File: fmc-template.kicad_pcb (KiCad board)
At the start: 6 copper layers, 84 x 69 mm, 31 parts, among them J19 WP Jumper, P1 ASP-134488-01, Q1 FDN335N, Q2 FDN335N, U9 AT24C64D

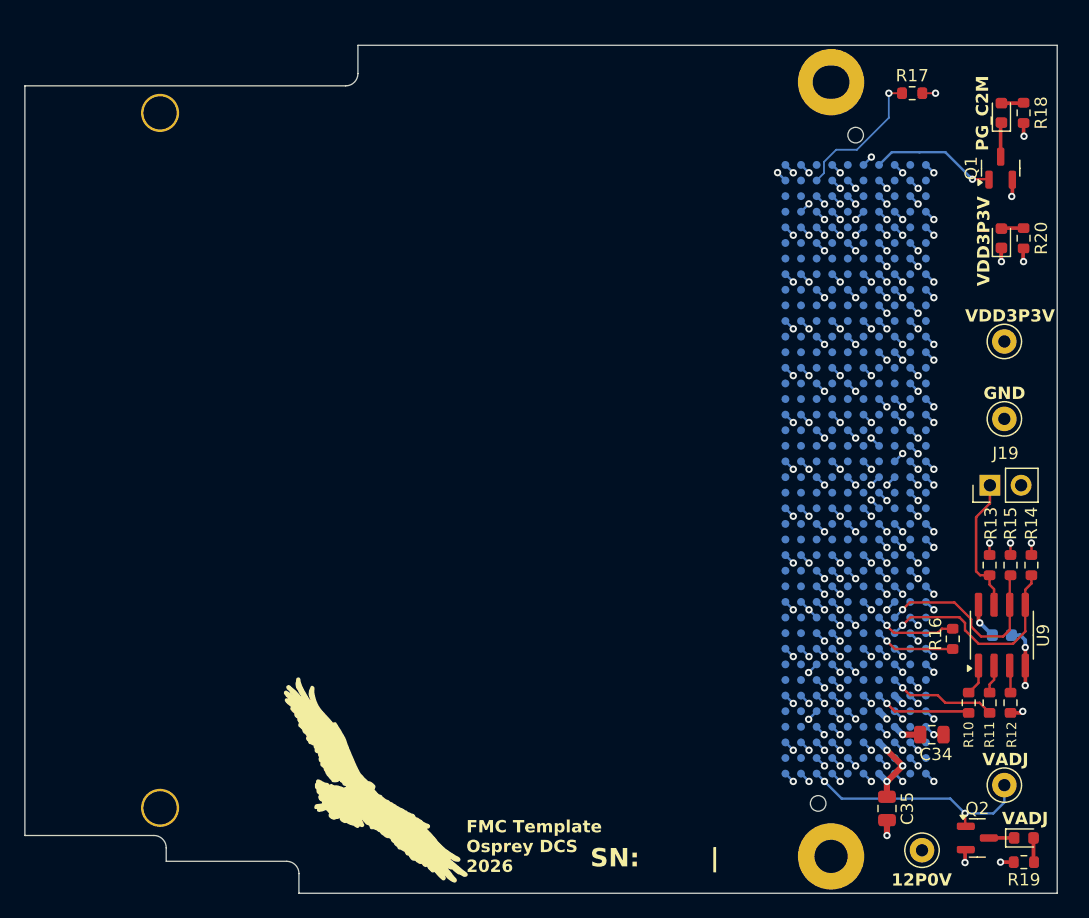
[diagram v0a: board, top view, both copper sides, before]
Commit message: Changed layout, added 12V and Heart LEDs
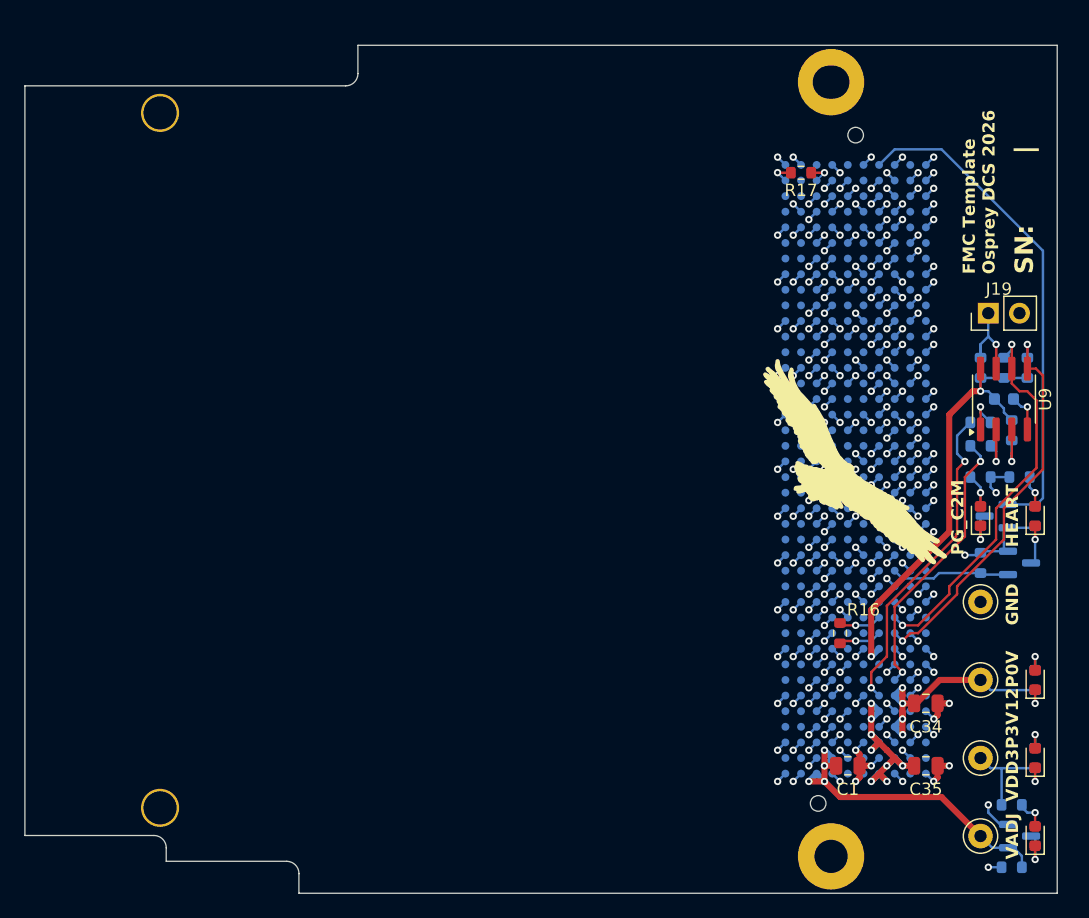
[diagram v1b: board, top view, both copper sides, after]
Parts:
- added C1: 22uF, Capacitor_SMD:C_0805_2012Metric, F.Cu at (174.0, 129.6)
- added D4: Green, LED_SMD:LED_0603_1608Metric, F.Cu at (189.2, 109.3)
- added D5: Green, LED_SMD:LED_0603_1608Metric, F.Cu at (189.2, 122.6)
- added Q3: FDN335N, Package_TO_SOT_SMD:SOT-23, B.Cu at (187.9, 113.1)
- added R1: 1k, Resistor_SMD:R_0603_1608Metric, B.Cu at (187.9, 106.1)
- added R2: 8.2k, Resistor_SMD:R_0603_1608Metric, B.Cu at (189.2, 122.6)
- added R3: 100k, Resistor_SMD:R_0603_1608Metric, B.Cu at (189.2, 109.3)
- added R4: 100k, Resistor_SMD:R_0603_1608Metric, B.Cu at (187.3, 137.9)
- added R5: 100k, Resistor_SMD:R_0603_1608Metric, B.Cu at (184.8, 113.1)
- D1, D2, D3: value LED_Green -> Green
- Q1, Q2, R10, R11, R12, R13, R14, R15, R18, R19, R20: moved to B.Cu
- moved Logo1 46.8 mm to (174.6, 105.5)
- moved D3 42.4 mm to (189.2, 129.0)
- moved R20 42.3 mm to (189.2, 129.0)
- moved TP3 34.0 mm to (184.8, 129.0)
- moved D1 32.9 mm to (184.8, 109.3)
- moved R18 29.8 mm to (184.8, 106.1), turned to 0 degrees
- moved Q1 28.3 mm to (186.0, 109.3), turned to 180 degrees
- moved R10 22.8 mm to (184.8, 101.7), turned to 0 degrees
- moved R12 22.2 mm to (187.3, 102.3), turned to -90 degrees
- moved R11 20.9 mm to (184.8, 103.6), turned to 0 degrees
- moved C33 19.2 mm to (186.7, 99.8)
- moved U9 19.2 mm to (186.7, 99.8)
- moved R13 16.1 mm to (184.8, 97.2), turned to 90 degrees
- moved R15 16.1 mm to (186.7, 97.2), turned to 90 degrees
- moved R14 16.1 mm to (188.6, 97.2), turned to 90 degrees
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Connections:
- net P1_12P0V renamed 12P0V
- net P1_3P3VAUX renamed 3P3VAUX
- net P1_PG_C2M renamed PG_C2M
- net P1_PRSNT renamed PRSNT
- net P1_TDI renamed TDI
- net P1_TDO renamed TDO
- net P1_VADJ renamed VADJ
- P1 pad C27: unconnected-(P1-PadC27) -> HEARTBEAT
- P1 pad C30: /FMC/EEPROM_SCL -> /EEPROM/SCL
- P1 pad C31: /FMC/EEPROM_SDA -> /EEPROM/SDA
- P1 pad C34: /FMC/EEPROM_GA0 -> /EEPROM/GA0
- P1 pad D35: /FMC/EEPROM_GA1 -> /EEPROM/GA1
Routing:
- net /EEPROM/SDA: track 0.00 -> 32.1 mm, vias 0 -> 2
- net /EEPROM/SCL: track 0.00 -> 31.6 mm, vias 0 -> 2
- net PG_C2M: track 10.3 -> 40.7 mm, vias 1 -> 0
- net 3P3VAUX: track 7.84 -> 37.1 mm, vias 6 -> 2
- net /EEPROM/GA1: track 0.00 -> 26.4 mm, vias 0 -> 2
- net /EEPROM/GA0: track 0.00 -> 22.8 mm, vias 0 -> 2
- net VDD3P3V: track 11.8 -> 31.0 mm, vias 7 -> 9
- net /FMC/EEPROM_SDA: track 17.6 -> 0.00 mm, vias 1 -> 0
- net 12P0V: track 3.42 -> 20.0 mm, vias 2 -> 4
- net /FMC/EEPROM_SCL: track 16.1 -> 0.00 mm, vias 1 -> 0
- net GND: track 156.4 -> 171.6 mm, vias 166 -> 168
- net HEARTBEAT: track 0.00 -> 9.80 mm
- net PRSNT: track 11.6 -> 1.98 mm
- net /FMC/EEPROM_GA0: track 8.83 -> 0.00 mm, vias 1 -> 0
- net VADJ: track 20.4 -> 29.1 mm, vias 3 -> 4
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- removed copper zone on In2.Cu, net 3P3VAUX
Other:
- board text added: "HEART"

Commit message: Add slotted mounting hole footprints for marble alignment
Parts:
- H1: footprint MountingHole:MountingHole_2.7mm_M2.5_Pad -> rf-input-fmc:MountingHole_3.0mm_M2.5_Pad_3.3mm_MarbleSlot
- H2: footprint rf-input-fmc:MountingHole_2.7mm_M2.5_Pad_Marble_Slot -> rf-input-fmc:MountingHole_3.0mm_M2.5_Pad_3.3mm_MarbleSlot
- H3, H4: footprint rf-input-fmc:MountingHole_2.7mm_Pad_3.1mm -> rf-input-fmc:MountingHole_3.0mm_3.8mm_Pad_3.3mm_MarbleSlot
